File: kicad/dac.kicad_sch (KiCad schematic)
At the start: 0 parts

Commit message: Added notes for DAC schematics
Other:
- note added: "Anti-Aliasing Filter and BNC Output Connector"
- note added: "DAC"
- note added: "MCP6001: I/O Rail-to-Rail, Single-Supply (1V8 to 5V), high-impedance input CMOS, low bias currents, unity gain stable"
- note added: "[3] ADC & Analog Front-End"
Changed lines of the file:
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@@
 		(rev "0.1")
 	)
+	(rectangle
+		(start 25.4 50.8)
+		(end 271.78 139.7)
+		(stroke
+			(width 0)
+			(type default)
+		)
+		(fill
+			(type none)
+		)
+	)
+	(text "DAC\n"
+		(exclude_from_sim no)
+		(at 28.702 47.498 0)
+		(effects
+			(font
+				(size 2.5 2.5)
+				(thickness 0.5)
+				(bold yes)
+			)
+		)
+	)
+	(text "[3] ADC & Analog Front-End"
+		(exclude_from_sim no)
+		(at 80.01 23.368 0)
+		(effects
+			(font
+				(size 5 5)
+				(thickness 1.2)
+				(bold yes)
+			)
+		)
+	)
+	(text "MCP6001: I/O Rail-to-Rail, Single-Supply (1V8 to 5V), high-impedance input CMOS, low bias currents, unity gain stable"
+		(exclude_from_sim no)
+		(at 112.522 37.592 0)
+		(effects
+			(font
+				(size 1.5 1.5)
+				(thickness 0.254)
+				(bold yes)
+			)
+			(justify left)
+		)
+	)
+	(text "Anti-Aliasing Filter and BNC Output Connector"
+		(exclude_from_sim no)
+		(at 227.33 46.99 0)
+		(effects
+			(font
+				(size 2.5 2.5)
+				(thickness 0.5)
+				(bold yes)
+			)
+		)
+	)
 )

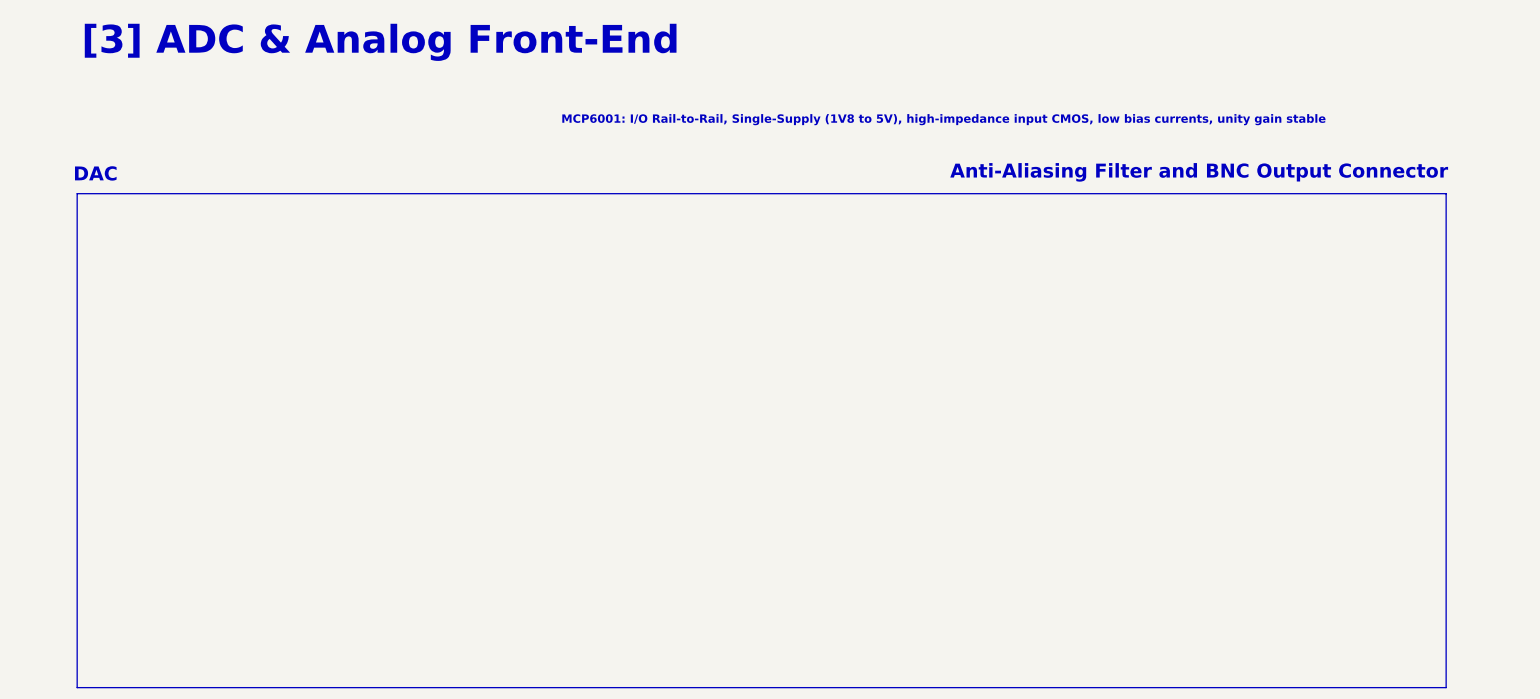
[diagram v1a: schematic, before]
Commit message: Updated parts numbering and notes
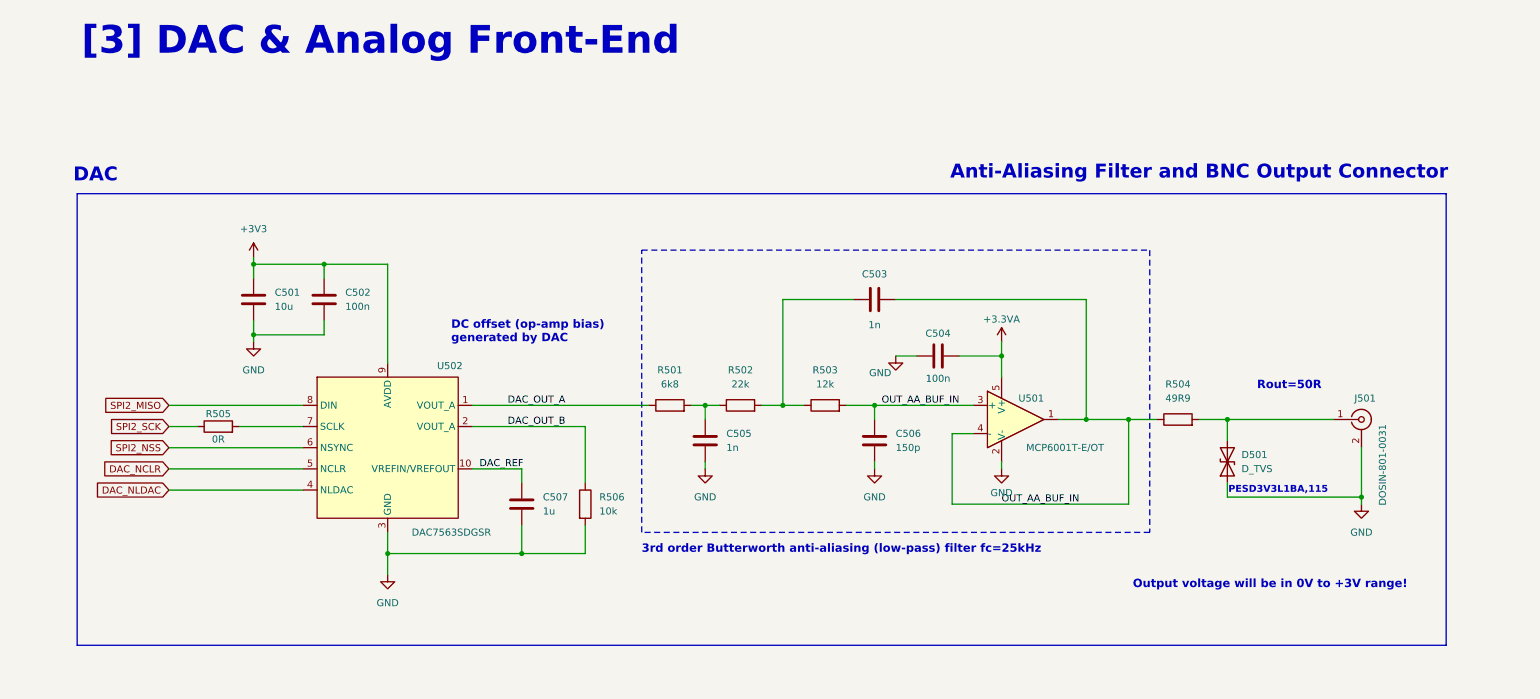
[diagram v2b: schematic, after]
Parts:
- added C501: 10u, symbol Device:C
- added C502, C504: 100n, symbol Device:C
- added C503, C505: 1n, symbol Device:C
- added C506: 150p, symbol Device:C
- added C507: 1u, symbol Device:C
- added D501: D_TVS, symbol CMF3216F-900-2P-T:D_TVS
- added J501: DOSIN-801-0031, symbol Connector:Conn_Coaxial
- added R501: 6k8, symbol Device:R
- added R502: 22k, symbol Device:R
- added R503: 12k, symbol Device:R
- added R504: 49R9, symbol Device:R
- added R505: 0R, symbol Device:R
- added R506: 10k, symbol Device:R
- added U501: MCP6001T-E/OT, Package_TO_SOT_SMD:SOT-23-5, symbol Amplifier_Operational:MCP6001-OT
- added U502: DAC7563SDGSR, symbol Analog_DAC:DAC7563
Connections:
- new net: C503.1, R502.2, R503.1
- new net: D501.2 (A2), J501.1 (In), R504.2
- new net: C505.1, R501.2, R502.1
- new net: R505.2, U502.7 (SCLK)
- new net +3.3VA: C504.2, U501.5 (V+)
- new net +3V3: C501.1, C502.1, U502.9 (AVDD)
- new net DAC_NCLR: U502.5 (NCLR)
- new net DAC_NLDAC: U502.4 (NLDAC)
- new net DAC_OUT_A: R501.1, U502.1 (VOUT_A)
- new net DAC_OUT_B: R506.1, U502.2 (VOUT_A)
- new net DAC_REF: C507.1, U502.10 (VREFIN/VREFOUT)
- new net GND: C501.2, C502.2, C504.1, C505.2, C506.2, C507.2, D501.1 (A1), J501.2 (Ext), R506.2, U501.2 (V-), U502.3 (GND)
- new net OUT_AA_BUF_IN: C503.2, C506.1, R503.2, R504.1, U501.1, U501.3 (+), U501.4 (-)
- new net SPI2_MISO: U502.8 (DIN)
- new net SPI2_NSS: U502.6 (NSYNC)
- new net SPI2_SCK: R505.1
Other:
- note added: "3rd order Butterworth anti-aliasing (low-pass) filter fc=25kHz"
- note added: "DC offset (op-amp bias) generated by DAC"
- note added: "Output voltage will be in 0V to +3V range!"
- note added: "PESD3V3L1BA,115"
- note added: "Rout=50R"
- note added: "[3] DAC & Analog Front-End"
- note removed: "MCP6001: I/O Rail-to-Rail, Single-Supply (1V8 to 5V), high-impedance input CMOS, low bias currents, unity gain stable"
- note removed: "[3] ADC & Analog Front-End"

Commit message: Save Progress
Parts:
- C501, C507: footprint (none) -> Capacitor_SMD:C_0603_1608Metric
- C502, C503, C504, C505, C506: footprint (none) -> Capacitor_SMD:C_0402_1005Metric
- D501: footprint (none) -> Diode_SMD:D_SOD-323
- R501, R502, R503, R504, R505, R506: footprint (none) -> Resistor_SMD:R_0402_1005Metric
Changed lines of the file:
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@@
 	)
 	(label "OUT_AA_BUF_IN"
-		(at 191.77 106.68 0)
+		(at 198.12 106.68 0)
 		(effects
 			(font
@@
 			)
 		)
-		(property "Footprint" ""
+		(property "Footprint" "Capacitor_SMD:C_0402_1005Metric"
 			(at 172.72 68.8848 0)
 			(effects
@@
 			)
 		)
-		(property "Footprint" ""
+		(property "Footprint" "Diode_SMD:D_SOD-323"
 			(at 232.41 99.06 0)
 			(effects
@@
 			)
 		)
-		(property "Footprint" ""
+		(property "Footprint" "Capacitor_SMD:C_0402_1005Metric"
 			(at 139.3952 99.06 0)
 			(effects
@@
 			)
 		)
-		(property "Footprint" ""
+		(property "Footprint" "Resistor_SMD:R_0402_1005Metric"
 			(at 160.02 90.678 90)
 			(effects
@@
 			)
 		)
-		(property "Footprint" ""
+		(property "Footprint" "Capacitor_SMD:C_0402_1005Metric"
 			(at 169.8752 99.06 0)
 			(effects
@@
 			)
 		)
-		(property "Footprint" ""
+		(property "Footprint" "Resistor_SMD:R_0402_1005Metric"
 			(at 50.8 94.488 90)
 			(effects
@@
 			)
 		)
-		(property "Footprint" ""
+		(property "Footprint" "Capacitor_SMD:C_0603_1608Metric"
 			(at 106.3752 110.49 0)
 			(effects
@@
 			)
 		)
-		(property "Footprint" ""
+		(property "Footprint" "Resistor_SMD:R_0402_1005Metric"
 			(at 223.52 93.218 90)
 			(effects
@@
 			)
 		)
-		(property "Footprint" ""
+		(property "Footprint" "Resistor_SMD:R_0402_1005Metric"
 			(at 144.78 90.678 90)
 			(effects
@@
 			)
 		)
-		(property "Footprint" ""
+		(property "Footprint" "Capacitor_SMD:C_0603_1608Metric"
 			(at 58.1152 73.66 0)
 			(effects
@@
 			)
 		)
-		(property "Footprint" ""
+		(property "Footprint" "Resistor_SMD:R_0402_1005Metric"
 			(at 115.062 106.68 90)
 			(effects
@@
 			)
 		)
-		(property "Footprint" ""
+		(property "Footprint" "Resistor_SMD:R_0402_1005Metric"
 			(at 132.08 90.678 90)
 			(effects
@@
 			)
 		)
-		(property "Footprint" ""
+		(property "Footprint" "Capacitor_SMD:C_0402_1005Metric"
 			(at 70.8152 73.66 0)
 			(effects
@@
 			)
 		)
-		(property "Footprint" ""
+		(property "Footprint" "Capacitor_SMD:C_0402_1005Metric"
 			(at 184.15 79.0448 0)
 			(effects
